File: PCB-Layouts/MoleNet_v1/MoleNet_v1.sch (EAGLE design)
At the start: 26 parts, among them IC1 25LC080P, K1 ISP, Q1 BS250, Q2 BS170, U1 MCP1703-5002E/DB, U3 RFM69CW, U4 ATMEGA328P-PU, X1 SMA-142-0701-851/861

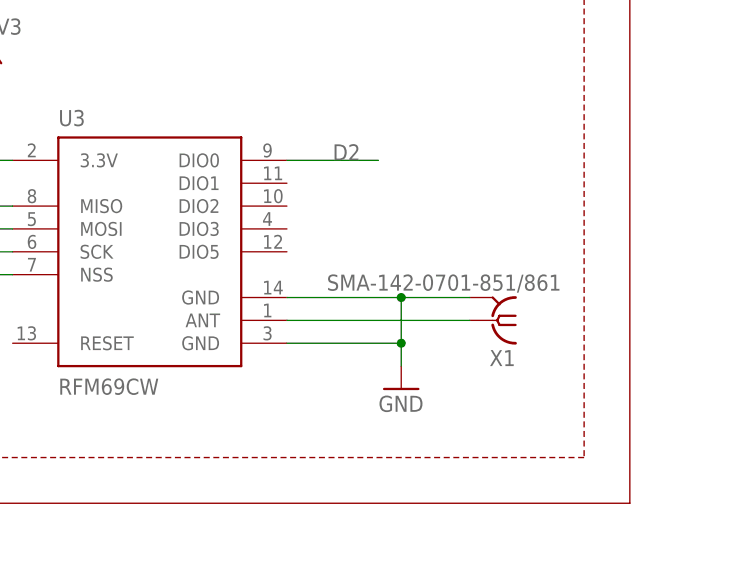
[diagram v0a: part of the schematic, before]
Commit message: corrected SMA connector of MoleNet v1
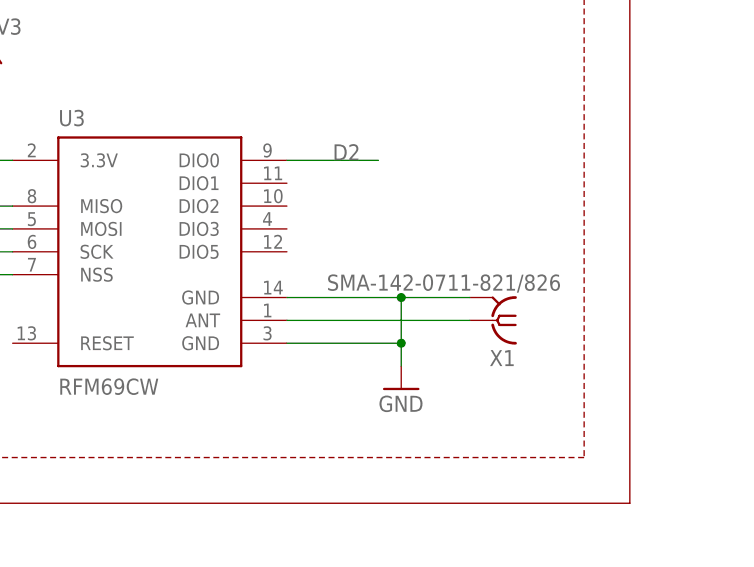
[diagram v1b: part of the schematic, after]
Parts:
- X1: value SMA-142-0701-851/861 -> SMA-142-0711-821/826; device con-coax:SMA-142-0701-851/861 -> con-coax:SMA-142-0711-821/826
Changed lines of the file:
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@@
 <part name="+3V3" library="supply1" deviceset="+3V3" device=""/>
 <part name="U3" library="SparkFun-RF" deviceset="RFM69" device="CW"/>
-<part name="X1" library="con-coax" deviceset="SMA-" device="142-0701-851/861"/>
+<part name="X1" library="con-coax" deviceset="SMA-" device="142-0711-821/826" value="SMA-142-0711-821/826"/>
 <part name="GND11" library="supply1" deviceset="GND" device=""/>
 <part name="+3V4" library="supply1" deviceset="+3V3" device=""/>

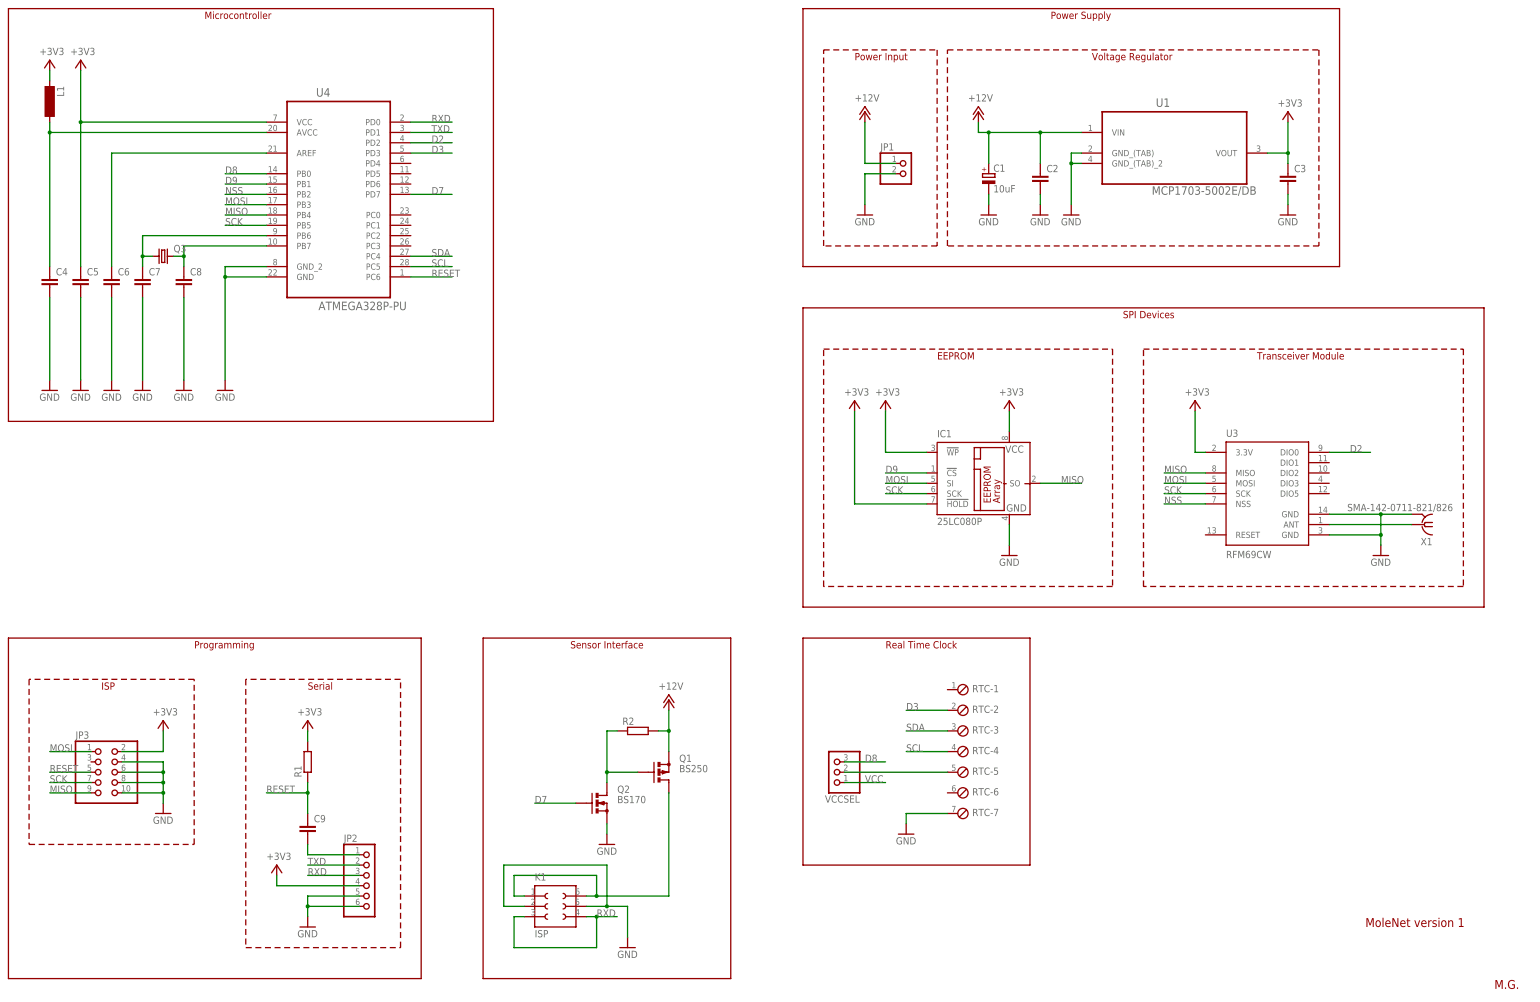
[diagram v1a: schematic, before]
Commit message: added/corrected part values in all layouts; created partlist for version 2.1
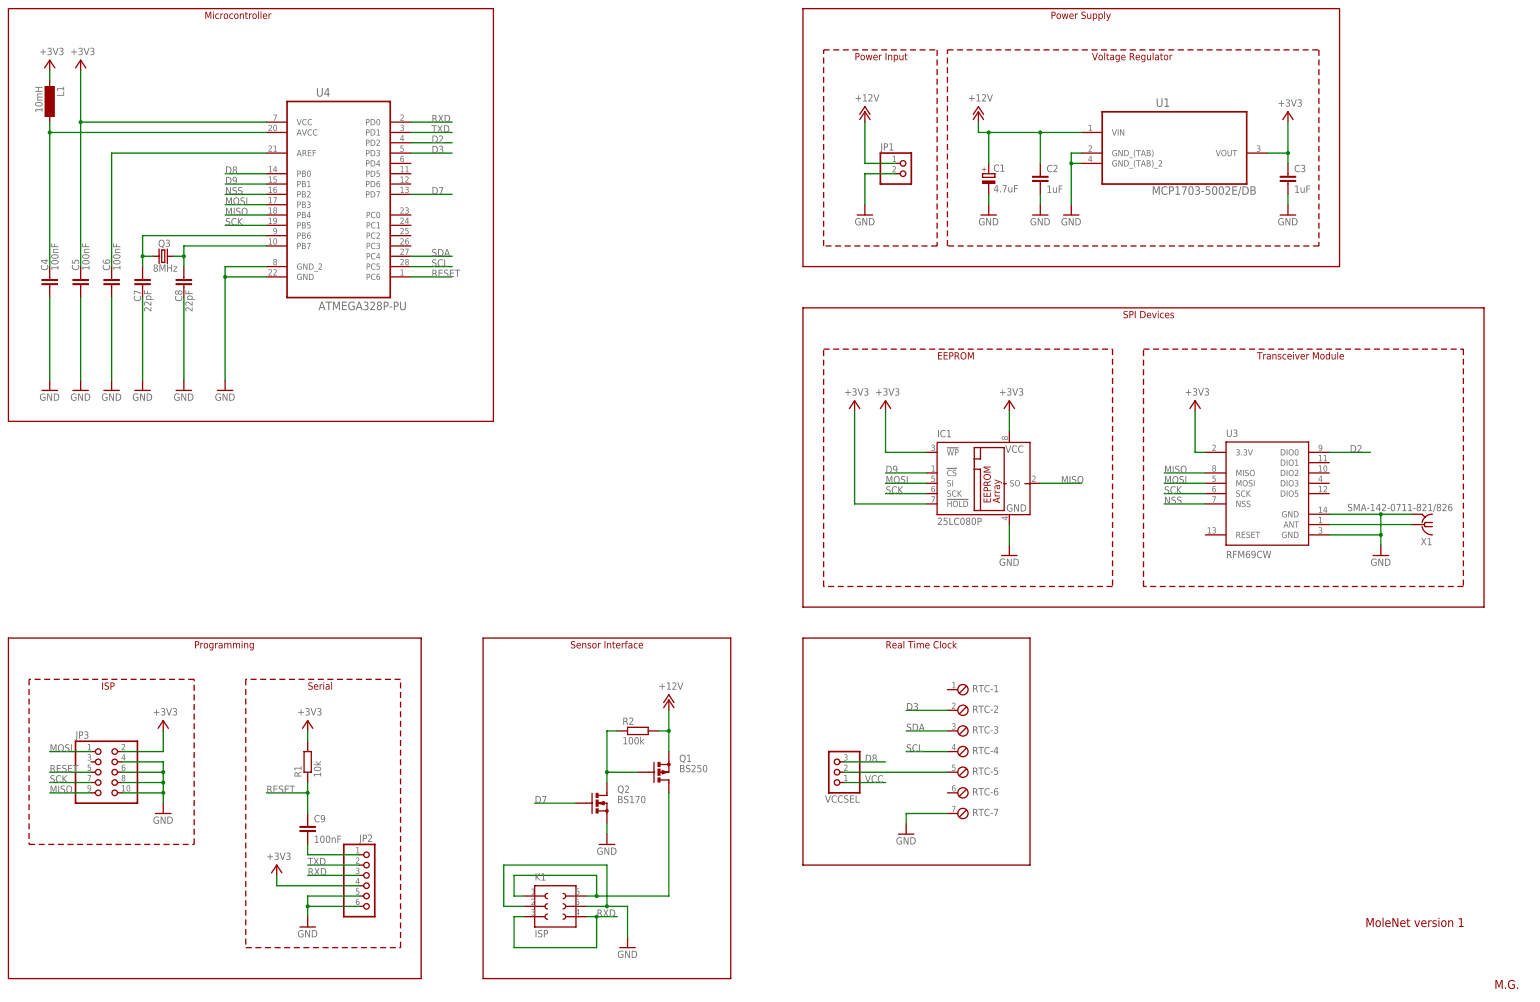
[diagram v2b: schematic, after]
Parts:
- C1: value 10uF -> 4.7uF
- C2, C3: value (none) -> 1uF
- C4, C5, C6, C9: value (none) -> 100nF
- C7, C8: value (none) -> 22pF
- L1: value (none) -> 10mH
- Q3: value (none) -> 8MHz
- R1: value (none) -> 10k
- R2: value (none) -> 100k
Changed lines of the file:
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@@
 <part name="Q1" library="transistor-small-signal" deviceset="BS250" device=""/>
 <part name="GND1" library="supply1" deviceset="GND" device=""/>
-<part name="R2" library="resistor" deviceset="R-EU_" device="0207/10"/>
+<part name="R2" library="resistor" deviceset="R-EU_" device="0207/10" value="100k"/>
 <part name="+3V1" library="supply1" deviceset="+3V3" device=""/>
 <part name="GND2" library="supply1" deviceset="GND" device=""/>
-<part name="L1" library="inductor-neosid" deviceset="BS" device="11"/>
-<part name="C1" library="resistor" deviceset="CPOL-EU" device="E2.5-6" value="10uF"/>
-<part name="C2" library="resistor" deviceset="C-EU" device="025-025X050"/>
-<part name="C3" library="resistor" deviceset="C-EU" device="025-025X050"/>
-<part name="C4" library="resistor" deviceset="C-EU" device="025-025X050"/>
+<part name="L1" library="inductor-neosid" deviceset="BS" device="11" value="10mH"/>
+<part name="C1" library="resistor" deviceset="CPOL-EU" device="E2.5-6" value="4.7uF"/>
+<part name="C2" library="resistor" deviceset="C-EU" device="025-025X050" value="1uF"/>
+<part name="C3" library="resistor" deviceset="C-EU" device="025-025X050" value="1uF"/>
+<part name="C4" library="resistor" deviceset="C-EU" device="025-025X050" value="100nF"/>
 <part name="GND3" library="supply1" deviceset="GND" device=""/>
-<part name="C6" library="resistor" deviceset="C-EU" device="025-025X050"/>
+<part name="C6" library="resistor" deviceset="C-EU" device="025-025X050" value="100nF"/>
 <part name="GND4" library="supply1" deviceset="GND" device=""/>
 <part name="+3V2" library="supply1" deviceset="+3V3" device=""/>
@@
 <part name="GND12" library="supply1" deviceset="GND" device=""/>
 <part name="FRAME1" library="frames" deviceset="A3L-LOC" device=""/>
-<part name="C5" library="resistor" deviceset="C-EU" device="025-025X050"/>
+<part name="C5" library="resistor" deviceset="C-EU" device="025-025X050" value="100nF"/>
 <part name="GND13" library="supply1" deviceset="GND" device=""/>
 <part name="JP2" library="pinhead" deviceset="PINHD-1X6" device=""/>
 <part name="GND14" library="supply1" deviceset="GND" device=""/>
 <part name="+3V8" library="supply1" deviceset="+3V3" device=""/>
-<part name="C9" library="resistor" deviceset="C-EU" device="025-025X050"/>
-<part name="R1" library="resistor" deviceset="R-EU_" device="0207/10"/>
+<part name="C9" library="resistor" deviceset="C-EU" device="025-025X050" value="100nF"/>
+<part name="R1" library="resistor" deviceset="R-EU_" device="0207/10" value="10k"/>
 <part name="+3V9" library="supply1" deviceset="+3V3" device=""/>
-<part name="Q3" library="crystal" deviceset="CRYSTAL" device="HC18U-V"/>
-<part name="C7" library="resistor" deviceset="C-EU" device="025-025X050"/>
-<part name="C8" library="resistor" deviceset="C-EU" device="025-025X050"/>
+<part name="Q3" library="crystal" deviceset="CRYSTAL" device="HC18U-V" value="8MHz"/>
+<part name="C7" library="resistor" deviceset="C-EU" device="025-025X050" value="22pF"/>
+<part name="C8" library="resistor" deviceset="C-EU" device="025-025X050" value="22pF"/>
 <part name="GND16" library="supply1" deviceset="GND" device=""/>
 <part name="GND17" library="supply1" deviceset="GND" device=""/>
@@
 <instance part="C2" gate="G$1" x="264.16" y="205.74"/>
 <instance part="C3" gate="G$1" x="325.12" y="205.74"/>
-<instance part="C4" gate="G$1" x="20.32" y="180.34"/>
+<instance part="C4" gate="G$1" x="20.32" y="180.34" smashed="yes">
+<attribute name="NAME" x="19.939" y="181.864" size="1.778" layer="95" rot="R90"/>
+<attribute name="VALUE" x="22.479" y="181.864" size="1.778" layer="96" rot="R90"/>
+</instance>
 <instance part="GND3" gate="1" x="20.32" y="152.4"/>
-<instance part="C6" gate="G$1" x="35.56" y="180.34"/>
+<instance part="C6" gate="G$1" x="35.56" y="180.34" smashed="yes">
+<attribute name="NAME" x="35.179" y="181.864" size="1.778" layer="95" rot="R90"/>
+<attribute name="VALUE" x="37.719" y="181.864" size="1.778" layer="96" rot="R90"/>
+</instance>
 <instance part="GND4" gate="1" x="35.56" y="152.4"/>
 <instance part="+3V2" gate="G$1" x="27.94" y="233.68" smashed="yes">
@@
 <instance part="GND12" gate="1" x="271.78" y="195.58"/>
 <instance part="FRAME1" gate="G$1" x="0" y="0"/>
-<instance part="C5" gate="G$1" x="27.94" y="180.34"/>
+<instance part="C5" gate="G$1" x="27.94" y="180.34" smashed="yes">
+<attribute name="NAME" x="27.559" y="181.864" size="1.778" layer="95" rot="R90"/>
+<attribute name="VALUE" x="30.099" y="181.864" size="1.778" layer="96" rot="R90"/>
+</instance>
 <instance part="GND13" gate="1" x="27.94" y="152.4"/>
-<instance part="JP2" gate="A" x="99.06" y="30.48"/>
+<instance part="JP2" gate="A" x="99.06" y="30.48" smashed="yes">
+<attribute name="NAME" x="96.52" y="41.275" size="1.778" layer="95"/>
+<attribute name="VALUE" x="92.71" y="20.32" size="1.778" layer="96"/>
+</instance>
 <instance part="GND14" gate="1" x="83.82" y="20.32"/>
 <instance part="+3V8" gate="G$1" x="76.2" y="35.56" smashed="yes">
@@
 <attribute name="VALUE" x="81.28" y="72.39" size="1.778" layer="96"/>
 </instance>
-<instance part="Q3" gate="G$1" x="48.26" y="185.42"/>
-<instance part="C7" gate="G$1" x="43.18" y="180.34"/>
-<instance part="C8" gate="G$1" x="53.34" y="180.34"/>
+<instance part="Q3" gate="G$1" x="48.26" y="185.42" smashed="yes">
+<attribute name="NAME" x="46.99" y="187.706" size="1.778" layer="95"/>
+<attribute name="VALUE" x="45.72" y="181.61" size="1.778" layer="96"/>
+</instance>
+<instance part="C7" gate="G$1" x="43.18" y="180.34" smashed="yes">
+<attribute name="NAME" x="42.799" y="174.244" size="1.778" layer="95" rot="R90"/>
+<attribute name="VALUE" x="45.339" y="171.704" size="1.778" layer="96" rot="R90"/>
+</instance>
+<instance part="C8" gate="G$1" x="53.34" y="180.34" smashed="yes">
+<attribute name="NAME" x="52.959" y="174.244" size="1.778" layer="95" rot="R90"/>
+<attribute name="VALUE" x="55.499" y="171.704" size="1.778" layer="96" rot="R90"/>
+</instance>
 <instance part="GND16" gate="1" x="43.18" y="152.4"/>
 <instance part="GND17" gate="1" x="53.34" y="152.4"/>
